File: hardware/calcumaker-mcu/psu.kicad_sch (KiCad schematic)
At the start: 21 parts, among them J1 USB-C, J2 BAT 1S Li-ion, Q1 AO3401A, U2 TPS63900DSKR, U3 USBLC6-2SC6, U4 MCP73831-2-OT

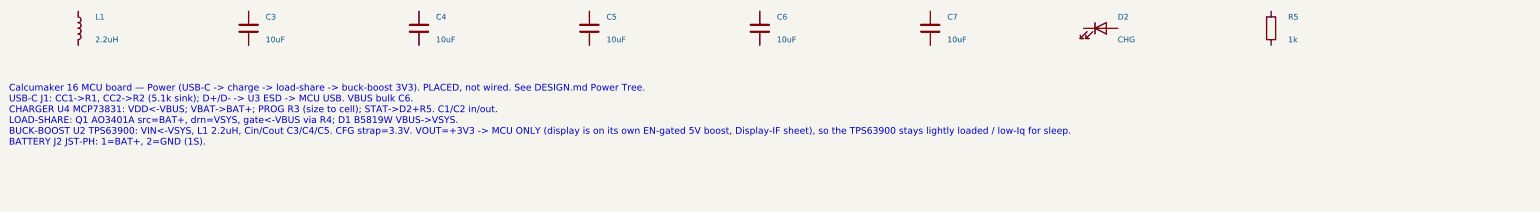
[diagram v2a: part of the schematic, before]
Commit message: hardware: MCU -> STM32U575RGT6 (LQFP-64) + 4MB QSPI flash; monospace wiring notes
MCU package + external flash
- Swap U1 STM32U575ZGT6 (LQFP-144) -> STM32U575RGT6 (LQFP-64, LCSC C5270980).
  The firmware links at ~323 KB so 1 MB flash is ample (~3x headroom), and with
  the key matrix scanned off-board the LQFP-64 has enough GPIO — smaller/cheaper.
- Correct the flash size everywhere: the STM32 `G` code = 1 MB (not 2 MB; the
  `I` parts are 2 MB). memory.x FLASH 2048K -> 1024K; .cargo runner -> RGTx.
- Add U7 W25Q32JVSSIQ, a 4 MB (32 Mbit) quad-SPI NOR (LCSC C179173, SOIC-8) on
  OCTOSPI1 as a new QSPIFlash sheet (+ R9 CS# pull-up + C26 decoupling) for
  memory-mapped (XIP) constants + state/program storage.
- mcu board 52 -> 55 components / 7 sheets. Docs (DESIGN.md, PARTS.md, READMEs,
  CLAUDE/AGENTS) updated; availability ladder now lists RGT6/VGT6/ZGT6.

Monospace, multi-line schematic wiring notes
- kschgen text_note() now renders notes in a monospace font (Courier New) so
  tables/columns line up; add note_block() + pin_table() helpers.
- Reformat all 14 per-sheet notes into titled, multi-line, aligned blocks —
  connector pinouts as PIN/SIGNAL tables, power/MCU sheets as wiring blocks.

The regenerated schematics carry both changes, so this is one commit. All three
boards regenerate + pass the structure check (mcu 55 / keyboard 119 / display
60, no duplicate refs).

Co-Authored-By: Claude Opus 4.8 (1M context) <noreply@anthropic.com>
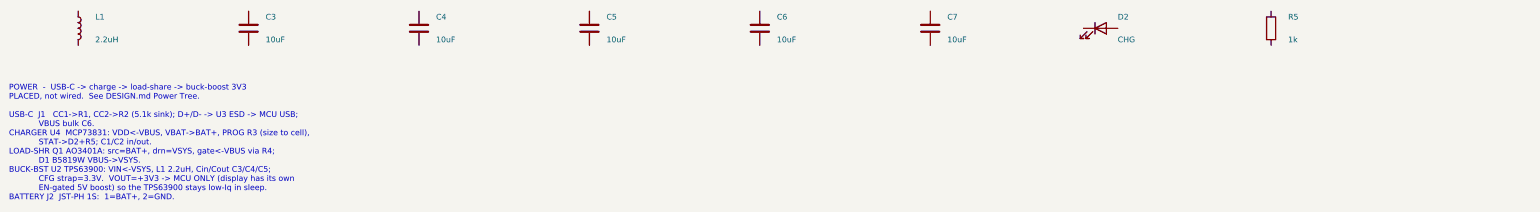
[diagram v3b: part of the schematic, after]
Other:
- note added: "POWER - USB-C -> charge -> load-share -> buck-boost 3V3 PLACED, not wired. See DESIGN.md Power Tree. USB-C J1 CC1->R1, CC2->R2 (5.1k sink); D+/D- -> U3 ESD -> MCU USB; VBUS bulk C6. CHARGER U4 MCP73831: VDD<-VBUS, VBAT->BAT+, PROG R3 (size to cell), STAT->D2+R5; C1/C2 in/out. LOAD-SHR Q1 AO3401A: src=BAT+, drn=VSYS, gate<-VBUS via R4; D1 B5819W VBUS->VSYS. BUCK-BST U2 TPS63900: VIN<-VSYS, L1 2.2u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"
- note removed: "Calcumaker 16 MCU board — Power (USB-C -> charge -> load-share -> buck-boost 3V3). PLACED, not wired. See DESIGN.md Power Tree. USB-C J1: CC1->R1, CC2->R2 (5.1k sink); D+/D- -> U3 ESD -> MCU USB. VBUS bulk C6. CHARGER U4 MCP73831: VDD<-VBUS; VBAT->BAT+; PROG R3 (size to cell); STAT->D2+R5. C1/C2 in/out. LOAD-SHARE: Q1 AO3401A src=BAT+, drn=VSYS, gate<-VBUS via R4; D1 B5819W VBUS->VSYS. BUCK-BOOST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"
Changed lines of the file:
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@@
 	(title_block
 		(title "Calcumaker 16 — MCU — USB-C / Li-ion charge / load-share / buck-boost")
-		(date "2026-07-05")
-		(rev "0.2")
+		(date "2026-07-06")
+		(rev "0.3")
 		(company "calcumaker authors")
 	)
@@
 		(instances
 			(project "calcumaker-mcu"
-				(path "/ca1c0000-0000-4000-8000-00000000ma01/672f4fa7-1cc1-4703-8edf-f066cdb44902"
+				(path "/ca1c0000-0000-4000-8000-00000000ma01/eb68b384-3231-4c3a-becc-31213731c008"
 					(reference "J1")
 					(unit 1)
@@
 		(instances
 			(project "calcumaker-mcu"
-				(path "/ca1c0000-0000-4000-8000-00000000ma01/672f4fa7-1cc1-4703-8edf-f066cdb44902"
+				(path "/ca1c0000-0000-4000-8000-00000000ma01/eb68b384-3231-4c3a-becc-31213731c008"
 					(reference "J2")
 					(unit 1)
@@
 		(instances
 			(project "calcumaker-mcu"
-				(path "/ca1c0000-0000-4000-8000-00000000ma01/672f4fa7-1cc1-4703-8edf-f066cdb44902"
+				(path "/ca1c0000-0000-4000-8000-00000000ma01/eb68b384-3231-4c3a-becc-31213731c008"
 					(reference "U2")
 					(unit 1)
@@
 		(instances
 			(project "calcumaker-mcu"
-				(path "/ca1c0000-0000-4000-8000-00000000ma01/672f4fa7-1cc1-4703-8edf-f066cdb44902"
+				(path "/ca1c0000-0000-4000-8000-00000000ma01/eb68b384-3231-4c3a-becc-31213731c008"
 					(reference "U3")
 					(unit 1)
@@
 		(instances
 			(project "calcumaker-mcu"
-				(path "/ca1c0000-0000-4000-8000-00000000ma01/672f4fa7-1cc1-4703-8edf-f066cdb44902"
+				(path "/ca1c0000-0000-4000-8000-00000000ma01/eb68b384-3231-4c3a-becc-31213731c008"
 					(reference "R1")
 					(unit 1)
@@
 		(instances
 			(project "calcumaker-mcu"
-				(path "/ca1c0000-0000-4000-8000-00000000ma01/672f4fa7-1cc1-4703-8edf-f066cdb44902"
+				(path "/ca1c0000-0000-4000-8000-00000000ma01/eb68b384-3231-4c3a-becc-31213731c008"
 					(reference "R2")
 					(unit 1)
@@
 		(instances
 			(project "calcumaker-mcu"
-				(path "/ca1c0000-0000-4000-8000-00000000ma01/672f4fa7-1cc1-4703-8edf-f066cdb44902"
+				(path "/ca1c0000-0000-4000-8000-00000000ma01/eb68b384-3231-4c3a-becc-31213731c008"
 					(reference "U4")
 					(unit 1)
@@
 		(instances
 			(project "calcumaker-mcu"
-				(path "/ca1c0000-0000-4000-8000-00000000ma01/672f4fa7-1cc1-4703-8edf-f066cdb44902"
+				(path "/ca1c0000-0000-4000-8000-00000000ma01/eb68b384-3231-4c3a-becc-31213731c008"
 					(reference "R3")
 					(unit 1)
@@
 		(instances
 			(project "calcumaker-mcu"
-				(path "/ca1c0000-0000-4000-8000-00000000ma01/672f4fa7-1cc1-4703-8edf-f066cdb44902"
+				(path "/ca1c0000-0000-4000-8000-00000000ma01/eb68b384-3231-4c3a-becc-31213731c008"
 					(reference "C1")
 					(unit 1)
@@
 		(instances
 			(project "calcumaker-mcu"
-				(path "/ca1c0000-0000-4000-8000-00000000ma01/672f4fa7-1cc1-4703-8edf-f066cdb44902"
+				(path "/ca1c0000-0000-4000-8000-00000000ma01/eb68b384-3231-4c3a-becc-31213731c008"
 					(reference "C2")
 					(unit 1)
@@
 		(instances
 			(project "calcumaker-mcu"
-				(path "/ca1c0000-0000-4000-8000-00000000ma01/672f4fa7-1cc1-4703-8edf-f066cdb44902"
+				(path "/ca1c0000-0000-4000-8000-00000000ma01/eb68b384-3231-4c3a-becc-31213731c008"
 					(reference "Q1")
 					(unit 1)
@@
 		(instances
 			(project "calcumaker-mcu"
-				(path "/ca1c0000-0000-4000-8000-00000000ma01/672f4fa7-1cc1-4703-8edf-f066cdb44902"
+				(path "/ca1c0000-0000-4000-8000-00000000ma01/eb68b384-3231-4c3a-becc-31213731c008"
 					(reference "D1")
 					(unit 1)
@@
 		(instances
 			(project "calcumaker-mcu"
-				(path "/ca1c0000-0000-4000-8000-00000000ma01/672f4fa7-1cc1-4703-8edf-f066cdb44902"
+				(path "/ca1c0000-0000-4000-8000-00000000ma01/eb68b384-3231-4c3a-becc-31213731c008"
 					(reference "R4")
 					(unit 1)
@@
 		(instances
 			(project "calcumaker-mcu"
-				(path "/ca1c0000-0000-4000-8000-00000000ma01/672f4fa7-1cc1-4703-8edf-f066cdb44902"
+				(path "/ca1c0000-0000-4000-8000-00000000ma01/eb68b384-3231-4c3a-becc-31213731c008"
 					(reference "L1")
 					(unit 1)
@@
 		(instances
 			(project "calcumaker-mcu"
-				(path "/ca1c0000-0000-4000-8000-00000000ma01/672f4fa7-1cc1-4703-8edf-f066cdb44902"
+				(path "/ca1c0000-0000-4000-8000-00000000ma01/eb68b384-3231-4c3a-becc-31213731c008"
 					(reference "C3")
 					(unit 1)
@@
 		(instances
 			(project "calcumaker-mcu"
-				(path "/ca1c0000-0000-4000-8000-00000000ma01/672f4fa7-1cc1-4703-8edf-f066cdb44902"
+				(path "/ca1c0000-0000-4000-8000-00000000ma01/eb68b384-3231-4c3a-becc-31213731c008"
 					(reference "C4")
 					(unit 1)
@@
 		(instances
 			(project "calcumaker-mcu"
-				(path "/ca1c0000-0000-4000-8000-00000000ma01/672f4fa7-1cc1-4703-8edf-f066cdb44902"
+				(path "/ca1c0000-0000-4000-8000-00000000ma01/eb68b384-3231-4c3a-becc-31213731c008"
 					(reference "C5")
 					(unit 1)
@@
 		(instances
 			(project "calcumaker-mcu"
-				(path "/ca1c0000-0000-4000-8000-00000000ma01/672f4fa7-1cc1-4703-8edf-f066cdb44902"
+				(path "/ca1c0000-0000-4000-8000-00000000ma01/eb68b384-3231-4c3a-becc-31213731c008"
 					(reference "C6")
 					(unit 1)
@@
 		(instances
 			(project "calcumaker-mcu"
-				(path "/ca1c0000-0000-4000-8000-00000000ma01/672f4fa7-1cc1-4703-8edf-f066cdb44902"
+				(path "/ca1c0000-0000-4000-8000-00000000ma01/eb68b384-3231-4c3a-becc-31213731c008"
 					(reference "C7")
 					(unit 1)
@@
 		(instances
 			(project "calcumaker-mcu"
-				(path "/ca1c0000-0000-4000-8000-00000000ma01/672f4fa7-1cc1-4703-8edf-f066cdb44902"
+				(path "/ca1c0000-0000-4000-8000-00000000ma01/eb68b384-3231-4c3a-becc-31213731c008"
 					(reference "D2")
 					(unit 1)
@@
 		(instances
 			(project "calcumaker-mcu"
-				(path "/ca1c0000-0000-4000-8000-00000000ma01/672f4fa7-1cc1-4703-8edf-f066cdb44902"
+				(path "/ca1c0000-0000-4000-8000-00000000ma01/eb68b384-3231-4c3a-becc-31213731c008"
 					(reference "R5")
 					(unit 1)
@@
 		)
 	)
-	(text "Calcumaker 16 MCU board — Power (USB-C -> charge -> load-share -> buck-boost 3V3). PLACED, not wired. See DESIGN.md Power Tree.\nUSB-C J1: CC1->R1, CC2->R2 (5.1k sink); D+/D- -> U3 ESD -> MCU USB. VBUS bulk C6.\nCHARGER U4 MCP73831: VDD<-VBUS; VBAT->BAT+; PROG R3 (size to cell); STAT->D2+R5. C1/C2 in/out.\nLOAD-SHARE: Q1 AO3401A src=BAT+, drn=VSYS, gate<-VBUS via R4; D1 B5819W VBUS->VSYS.\nBUCK-BOOST U2 TPS63900: VIN<-VSYS, L1 2.2uH, Cin/Cout C3/C4/C5. CFG strap=3.3V. VOUT=+3V3 -> MCU ONLY (display is on its own EN-gated 5V boost, Display-IF sheet), so the TPS63900 stays lightly loaded / low-Iq for sleep.\nBATTERY J2 JST-PH: 1=BAT+, 2=GND (1S)."
+	(text "POWER  -  USB-C -> charge -> load-share -> buck-boost 3V3\nPLACED, not wired.  See DESIGN.md Power Tree.\n\nUSB-C  J1   CC1->R1, CC2->R2 (5.1k sink); D+/D- -> U3 ESD -> MCU USB;\n            VBUS bulk C6.\nCHARGER U4  MCP73831: VDD<-VBUS, VBAT->BAT+, PROG R3 (size to cell),\n            STAT->D2+R5; C1/C2 in/out.\nLOAD-SHR Q1 AO3401A: src=BAT+, drn=VSYS, gate<-VBUS via R4;\n            D1 B5819W VBUS->VSYS.\nBUCK-BST U2 TPS63900: VIN<-VSYS, L1 2.2uH, Cin/Cout C3/C4/C5;\n            CFG strap=3.3V.  VOUT=+3V3 -> MCU ONLY (display has its own\n            EN-gated 5V boost) so the TPS63900 stays low-Iq in sleep.\nBATTERY J2  JST-PH 1S:  1=BAT+, 2=GND."
 		(exclude_from_sim no)
 		(at 15.00 165.00 0)
-		(effects (font (size 1.5 1.5)) (justify left top))
+		(effects (font (face "Courier New") (size 1.27 1.27)) (justify left top))
 	)
 	(sheet_instances

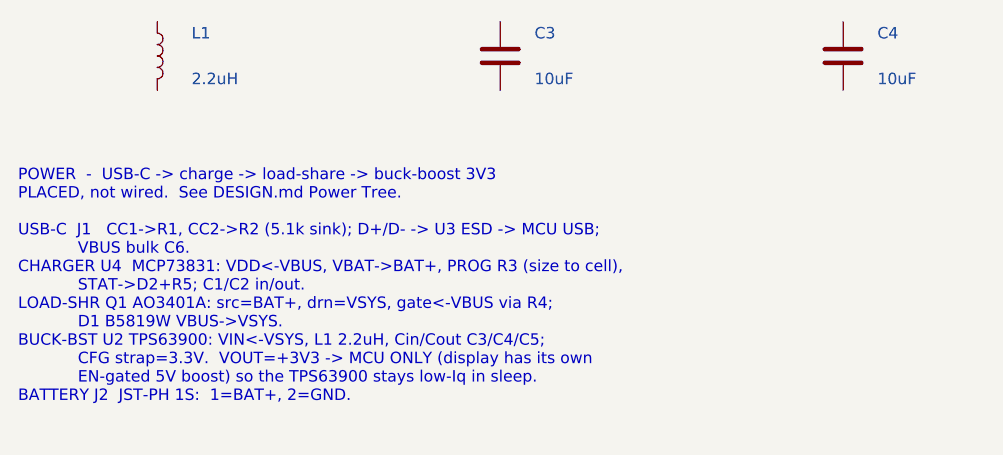
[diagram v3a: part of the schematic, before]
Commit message: hardware: per-key RGB hint lighting on the keyboard board (50x SK6805 on gated VSYS) (#4)
Add addressable RGB accent lighting that hints key positions / presses -- one
SK6805-EC15 (1.5x1.5mm, the smallest serial RGB with a KiCad footprint + real
LCSC stock, C2890035) beside each of the 50 keys, single-wire daisy chain off
one STM32G0 pin.

Power: the LEDs are ~5V parts and the keyboard rail is only 3.3V, so they run
off VSYS (the MCU board's load-shared battery/USB rail, ~3.7-4.7V) brought up a
WIDENED 12-pin mezzanine (10 -> 12: +VSYS +GND). A high-side P-FET load switch
(Q1 AO3401A + Q2 2N7002) gates the whole LED rail off in sleep (G0 LED_EN) to
protect battery life, and a 74LVC1G125 (powered from the gated rail) level-shifts
the 3.3V data up to the LED VIH.

- calcumaker-keyboard: new KeyLighting sheet (50x SK6805 D56-D105 + U2 shifter +
  Q1/Q2 load switch + R7-R10 / C6-C7); J1 mezzanine -> 12-pin DF40C-12DP
  (C6224952). 119 -> 178 components.
- calcumaker-mcu: J5 mezzanine -> 12-pin DF40B-12DS (C3641147); route VSYS.
- DF40 stack: the receptacle SUFFIX sets the mated height (none = 1.5mm,
  (2.0) = 2.0mm, H-series = 2.5-4.0mm), NOT the B/C letter; the DF40C plug is the
  common header -- so DF40C-12DP x DF40B-12DS is a valid 1.5mm stack, same as the
  original 10-pin (DF40C-12DS just isn't LCSC-stocked).
- DESIGN.md / PARTS.md / memory: RGB subsystem, 12-pin pinout, BOM rows, the
  sleep-gate + current-cap notes (firmware must cap total brightness; 50x
  full-white ~0.75A would exceed the DF40 / VSYS budget).

All three boards regenerate + pass the structure check (mcu 55 / keyboard 178 /
display 60, no duplicate refs).

Co-authored-by: Claude Opus 4.8 (1M context) <noreply@anthropic.com>
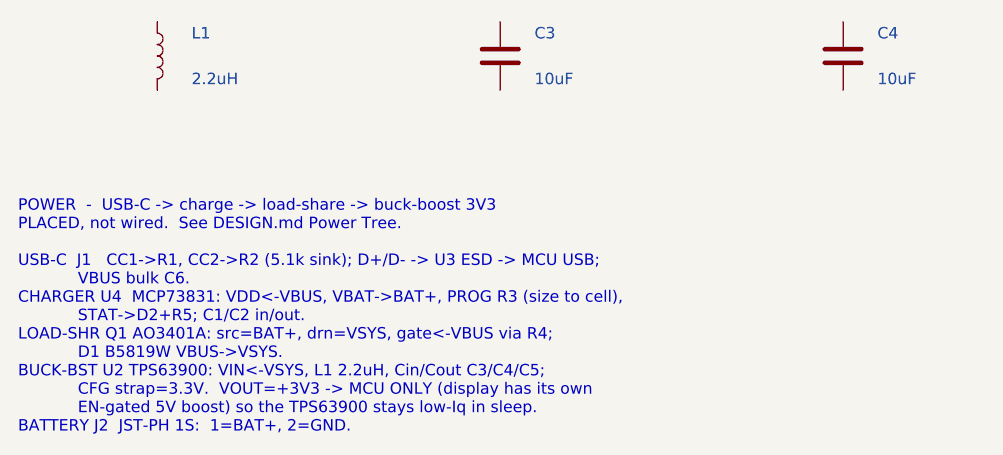
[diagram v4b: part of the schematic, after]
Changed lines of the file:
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@@
 	(text "POWER  -  USB-C -> charge -> load-share -> buck-boost 3V3\nPLACED, not wired.  See DESIGN.md Power Tree.\n\nUSB-C  J1   CC1->R1, CC2->R2 (5.1k sink); D+/D- -> U3 ESD -> MCU USB;\n            VBUS bulk C6.\nCHARGER U4  MCP73831: VDD<-VBUS, VBAT->BAT+, PROG R3 (size to cell),\n            STAT->D2+R5; C1/C2 in/out.\nLOAD-SHR Q1 AO3401A: src=BAT+, drn=VSYS, gate<-VBUS via R4;\n            D1 B5819W VBUS->VSYS.\nBUCK-BST U2 TPS63900: VIN<-VSYS, L1 2.2uH, Cin/Cout C3/C4/C5;\n            CFG strap=3.3V.  VOUT=+3V3 -> MCU ONLY (display has its own\n            EN-gated 5V boost) so the TPS63900 stays low-Iq in sleep.\nBATTERY J2  JST-PH 1S:  1=BAT+, 2=GND."
 		(exclude_from_sim no)
-		(at 15.00 165.00 0)
+		(at 15.00 168.40 0)
 		(effects (font (face "Courier New") (size 1.27 1.27)) (justify left top))
 	)
